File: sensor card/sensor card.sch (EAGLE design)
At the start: 21 parts, among them J1 8-1393644-0, J2 MJ-3536N, J3 MJ-3536N, X1 S4B-XH-A, X2 S4B-XH-A

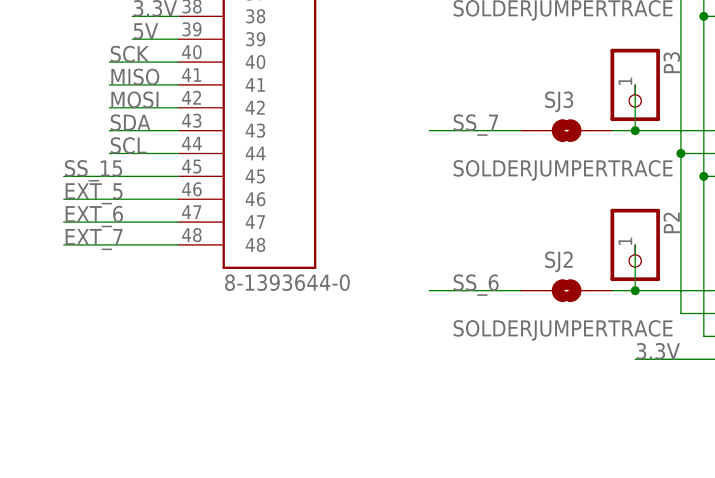
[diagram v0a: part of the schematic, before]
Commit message: fixed library attributes for the din41612 connector, fixed git problems
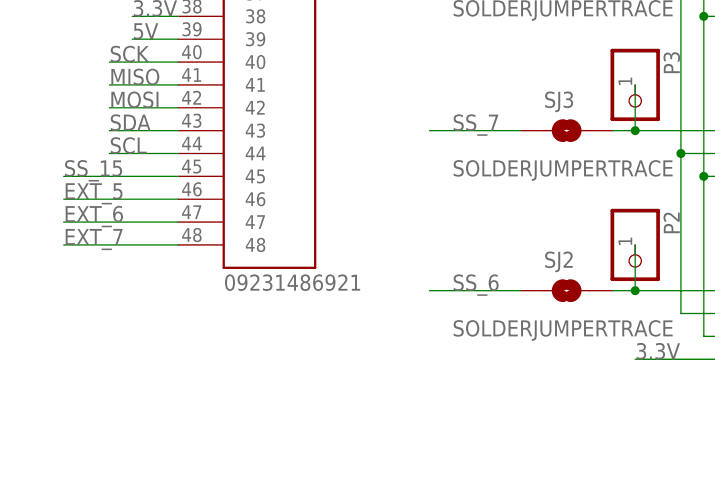
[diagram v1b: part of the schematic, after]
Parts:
- J1: value 8-1393644-0 -> 09231486921; device 8-1393644-0:8-1393644-0 -> din41612_48_pin_board:09231486921
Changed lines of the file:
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@@
 </classes>
 <parts>
-<part name="J1" library="8-1393644-0" deviceset="8-1393644-0" device=""/>
+<part name="J1" library="din41612_48_pin_board" deviceset="09231486921" device=""/>
 <part name="GND1" library="supply1" library_urn="urn:adsk.eagle:library:371" deviceset="GND" device=""/>
 <part name="GND2" library="supply1" library_urn="urn:adsk.eagle:library:371" deviceset="GND" device=""/>

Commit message: added cam data
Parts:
- U$1, U$3, U$4, U$5: value SCCDRRV100MDSA3SSCDRRV100MDSA3 -> SSCDRRV100MDSA3
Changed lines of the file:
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@@
 <part name="GND2" library="supply1" library_urn="urn:adsk.eagle:library:371" deviceset="GND" device=""/>
 <part name="GND3" library="supply1" library_urn="urn:adsk.eagle:library:371" deviceset="GND" device=""/>
-<part name="U$1" library="SCCDRRV100MDSA3" deviceset="SCCDRRV100MDSA3" device="SSCDRRV100MDSA3" package3d_urn="urn:adsk.eagle:package:23793141/1"/>
+<part name="U$1" library="SCCDRRV100MDSA3" deviceset="SCCDRRV100MDSA3" device="SSCDRRV100MDSA3" package3d_urn="urn:adsk.eagle:package:23793141/1" value="SSCDRRV100MDSA3"/>
 <part name="U$2" library="MCP346XRT-E:ST" deviceset="MCP346X-E/ST" device=""/>
 <part name="GND4" library="supply1" library_urn="urn:adsk.eagle:library:371" deviceset="GND" device=""/>
@@
 <part name="P1" library="pinhead" library_urn="urn:adsk.eagle:library:325" deviceset="PINHD-1X1" device="" package3d_urn="urn:adsk.eagle:package:22485/2"/>
 <part name="SJ1" library="SparkFun-Passives" deviceset="SOLDERJUMPER" device="TRACE"/>
-<part name="U$3" library="SCCDRRV100MDSA3" deviceset="SCCDRRV100MDSA3" device="SSCDRRV100MDSA3" package3d_urn="urn:adsk.eagle:package:23793141/1"/>
-<part name="U$4" library="SCCDRRV100MDSA3" deviceset="SCCDRRV100MDSA3" device="SSCDRRV100MDSA3" package3d_urn="urn:adsk.eagle:package:23793141/1"/>
-<part name="U$5" library="SCCDRRV100MDSA3" deviceset="SCCDRRV100MDSA3" device="SSCDRRV100MDSA3" package3d_urn="urn:adsk.eagle:package:23793141/1"/>
+<part name="U$3" library="SCCDRRV100MDSA3" deviceset="SCCDRRV100MDSA3" device="SSCDRRV100MDSA3" package3d_urn="urn:adsk.eagle:package:23793141/1" value="SSCDRRV100MDSA3"/>
+<part name="U$4" library="SCCDRRV100MDSA3" deviceset="SCCDRRV100MDSA3" device="SSCDRRV100MDSA3" package3d_urn="urn:adsk.eagle:package:23793141/1" value="SSCDRRV100MDSA3"/>
+<part name="U$5" library="SCCDRRV100MDSA3" deviceset="SCCDRRV100MDSA3" device="SSCDRRV100MDSA3" package3d_urn="urn:adsk.eagle:package:23793141/1" value="SSCDRRV100MDSA3"/>
 <part name="X1" library="con-JST XH" deviceset="S4B-XH" device="-A"/>
 <part name="X2" library="con-JST XH" deviceset="S4B-XH" device="-A"/>
